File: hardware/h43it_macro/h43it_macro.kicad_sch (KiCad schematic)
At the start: 25 parts, among them J1 Conn_01x04_Pin, SW1 SW_Push, SW2 SW_Push

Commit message: updates
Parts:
- added D17, D18, D19, D20, D21, D22, D23, D24, D25, D26, D27, D28, D29, D30, D31, D32: LED, LED_SMD:LED_0805_2012Metric, symbol Device:LED
- added U1: ATtiny816-M, Package_DFN_QFN:VQFN-20-1EP_3x3mm_P0.4mm_EP1.7x1.7mm, symbol MCU_Microchip_ATtiny:ATtiny816-M
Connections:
- net A+: now also R1.2; no longer R1.1
- net B+: now also R2.2; no longer R2.1
- net C+: now also R3.2; no longer R3.1
- net D+: now also R4.2; no longer R4.1
- net GND: now also U1.21 (GND), U1.3 (GND)
- net M-: now also D21.1 (K), D29.1 (K); no longer D5.1 (K), D9.1 (K)
- net N-: now also D22.1 (K), D30.1 (K); no longer D10.1 (K), D6.1 (K)
- net O-: now also D23.1 (K), D31.1 (K); no longer D11.1 (K), D7.1 (K)
- net P-: now also D24.1 (K), D32.1 (K); no longer D12.1 (K), D8.1 (K)
- net TX: now also U1.12 (PB2)
- net UPDI: now also U1.19 (~{RESET}/PA0)
- net VCC: now also U1.4 (VCC)
- net at D10.2 (A), D11.2 (A), D12.2 (A)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: now also D13.2 (A), D14.2 (A), D15.2 (A), D16.2 (A), R2.1; no longer R3.2
- net at D1.2 (A), D2.2 (A), D3.2 (A)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: now also D5.2 (A), D6.2 (A), D7.2 (A), D8.2 (A), R1.1; no longer R1.2
- new net: D17.2 (A), D18.2 (A), D19.2 (A), D20.2 (A), D21.2 (A), D22.2 (A), D23.2 (A), D24.2 (A), R3.1
- new net: D25.2 (A), D26.2 (A), D27.2 (A), D28.2 (A), D29.2 (A), D30.2 (A), D31.2 (A), D32.2 (A), R4.1
- new net Q-: D17.1 (K), D25.1 (K), D5.1 (K), D9.1 (K)
- new net R-: D10.1 (K), D18.1 (K), D26.1 (K), D6.1 (K)
- new net S-: D11.1 (K), D19.1 (K), D27.1 (K), D7.1 (K)
- new net T-: D12.1 (K), D20.1 (K), D28.1 (K), D8.1 (K)
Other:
- moved on the sheet: D1, D2, D3, D4, R1

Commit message: schematic draft finsihed
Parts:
- added D33: LED, LED_SMD:LED_0805_2012Metric, symbol Device:LED
- added R5: 100Ω, Resistor_SMD:R_0805_2012Metric, symbol Device:R_US
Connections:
- net A+: now also U1.15 (PC0)
- net B+: now also U1.16 (PC1)
- net C+: now also U1.17 (PC2)
- net D+: now also U1.18 (PC3)
- net GND: now also D33.1 (K)
- net M-: now also U1.14 (PB0)
- net N-: now also U1.13 (PB1)
- net O-: now also U1.12 (PB2)
- net P-: now also U1.11 (PB3)
- net Q-: now also U1.10 (PB4)
- net R-: now also U1.9 (PB5)
- net S-: now also U1.7 (PA6)
- net SW: now also U1.5 (PA4)
- net T-: now also U1.8 (PA7)
- net TX: now also U1.20 (PA1); no longer U1.12 (PB2)
- net LED_ind: now reaches U1.6 (PA5)
- net LED_ind: now also R5.2
- new net: D33.2 (A), R5.1
- no-connect marks 0 -> 2
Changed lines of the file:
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@@
   (junction (at 81.28 157.48) (diameter 0) (color 0 0 0 0)
   )
-  (wire (pts (xy 184.15 109.22) (xy 181.61 109.22))
-    (stroke (width 0) (type default))
-  )
+  (no_connect (at 181.61 88.9))
+  (no_connect (at 181.61 86.36))
   (wire (pts (xy 48.26 107.95) (xy 52.07 107.95))
     (stroke (width 0) (type default))
@@
     (stroke (width 0) (type default))
   )
+  (wire (pts (xy 191.77 44.45) (xy 187.96 44.45))
+    (stroke (width 0) (type default))
+  )
   (wire (pts (xy 132.08 44.45) (xy 133.35 44.45))
     (stroke (width 0) (type default))
@@
     (effects (font (size 1.27 1.27)) (justify left bottom))
   )
-  (label "TX" (at 184.15 109.22 0) (fields_autoplaced)
+  (label "N-" (at 181.61 106.68 0) (fields_autoplaced)
+    (effects (font (size 1.27 1.27)) (justify left bottom))
+  )
+  (label "TX" (at 181.61 83.82 0) (fields_autoplaced)
     (effects (font (size 1.27 1.27)) (justify left bottom))
   )
@@
     (effects (font (size 1.27 1.27)) (justify left bottom))
   )
+  (label "GND" (at 191.77 44.45 0) (fields_autoplaced)
+    (effects (font (size 1.27 1.27)) (justify left bottom))
+  )
   (label "T-" (at 50.8 182.88 0) (fields_autoplaced)
     (effects (font (size 1.27 1.27)) (justify left bottom))
@@
     (effects (font (size 1.27 1.27)) (justify left bottom))
   )
+  (label "SW" (at 181.61 91.44 0) (fields_autoplaced)
+    (effects (font (size 1.27 1.27)) (justify left bottom))
+  )
   (label "B+" (at 39.37 82.55 0) (fields_autoplaced)
     (effects (font (size 1.27 1.27)) (justify left bottom))
   )
+  (label "O-" (at 181.61 109.22 0) (fields_autoplaced)
+    (effects (font (size 1.27 1.27)) (justify left bottom))
+  )
   (label "M-" (at 52.07 95.25 0) (fields_autoplaced)
     (effects (font (size 1.27 1.27)) (justify left bottom))
@@
     (effects (font (size 1.27 1.27)) (justify left bottom))
   )
+  (label "A+" (at 151.13 104.14 180) (fields_autoplaced)
+    (effects (font (size 1.27 1.27)) (justify right bottom))
+  )
   (label "T-" (at 69.85 182.88 0) (fields_autoplaced)
     (effects (font (size 1.27 1.27)) (justify left bottom))
@@
     (effects (font (size 1.27 1.27)) (justify left bottom))
   )
+  (label "S-" (at 181.61 96.52 0) (fields_autoplaced)
+    (effects (font (size 1.27 1.27)) (justify left bottom))
+  )
   (label "S-" (at 29.21 170.18 0) (fields_autoplaced)
     (effects (font (size 1.27 1.27)) (justify left bottom))
@@
     (effects (font (size 1.27 1.27)) (justify left bottom))
   )
+  (label "P-" (at 181.61 111.76 0) (fields_autoplaced)
+    (effects (font (size 1.27 1.27)) (justify left bottom))
+  )
+  (label "Q-" (at 181.61 114.3 0) (fields_autoplaced)
+    (effects (font (size 1.27 1.27)) (justify left bottom))
+  )
+  (label "D+" (at 151.13 111.76 180) (fields_autoplaced)
+    (effects (font (size 1.27 1.27)) (justify right bottom))
+  )
   (label "A+" (at 17.78 82.55 0) (fields_autoplaced)
     (effects (font (size 1.27 1.27)) (justify left bottom))
@@
     (effects (font (size 1.27 1.27)) (justify left bottom))
   )
+  (label "T-" (at 181.61 99.06 0) (fields_autoplaced)
+    (effects (font (size 1.27 1.27)) (justify left bottom))
+  )
+  (label "LED_ind" (at 181.61 93.98 0) (fields_autoplaced)
+    (effects (font (size 1.27 1.27)) (justify left bottom))
+  )
   (label "N-" (at 30.48 107.95 0) (fields_autoplaced)
     (effects (font (size 1.27 1.27)) (justify left bottom))
@@
     (effects (font (size 1.27 1.27)) (justify left bottom))
   )
+  (label "C+" (at 151.13 109.22 180) (fields_autoplaced)
+    (effects (font (size 1.27 1.27)) (justify right bottom))
+  )
   (label "O-" (at 71.12 120.65 0) (fields_autoplaced)
     (effects (font (size 1.27 1.27)) (justify left bottom))
   )
+  (label "B+" (at 151.13 106.68 180) (fields_autoplaced)
+    (effects (font (size 1.27 1.27)) (justify right bottom))
+  )
+  (label "LED_ind" (at 172.72 44.45 180) (fields_autoplaced)
+    (effects (font (size 1.27 1.27)) (justify right bottom))
+  )
+  (label "M-" (at 181.61 104.14 0) (fields_autoplaced)
+    (effects (font (size 1.27 1.27)) (justify left bottom))
+  )
   (label "UPDI" (at 181.61 81.28 0) (fields_autoplaced)
     (effects (font (size 1.27 1.27)) (justify left bottom))
@@
   )
   (label "M-" (at 30.48 95.25 0) (fields_autoplaced)
+    (effects (font (size 1.27 1.27)) (justify left bottom))
+  )
+  (label "R-" (at 181.61 116.84 0) (fields_autoplaced)
     (effects (font (size 1.27 1.27)) (justify left bottom))
   )
@@
     )
   )
+  (symbol (lib_id "Device:LED") (at 184.15 44.45 180) (unit 1)
+    (in_bom yes) (on_board yes) (dnp no) (fields_autoplaced)
+    (property "Reference" "D33" (at 185.7375 50.8 0)
+      (effects (font (size 1.27 1.27)))
+    )
+    (property "Value" "LED" (at 185.7375 48.26 0)
+      (effects (font (size 1.27 1.27)))
+    )
+    (property "Footprint" "LED_SMD:LED_0805_2012Metric" (at 184.15 44.45 0)
+      (effects (font (size 1.27 1.27)) hide)
+    )
+    (property "Datasheet" "~" (at 184.15 44.45 0)
+      (effects (font (size 1.27 1.27)) hide)
+    )
+    (pin "2")
+    (pin "1")
+    (instances
+      (project "h43it_macro"
+        (path "/37d2c260-87ad-48ae-8c36-e59ae5413c59"
+          (reference "D33") (unit 1)
+        )
+      )
+    )
+  )
   (symbol (lib_id "Device:LED") (at 86.36 120.65 180) (unit 1)
     (in_bom yes) (on_board yes) (dnp no) (fields_autoplaced)
@@
         )
       )
+    )
+  )
+  (symbol (lib_id "Device:R_US") (at 176.53 44.45 270) (unit 1)
+    (in_bom yes) (on_board yes) (dnp no) (fields_autoplaced)
+    (property "Reference" "R5" (at 176.53 38.1 90)
+      (effects (font (size 1.27 1.27)))
+    )
+    (property "Value" "100Ω" (at 176.53 40.64 90)
+      (effects (font (size 1.27 1.27)))
+    )
+    (property "Footprint" "Resistor_SMD:R_0805_2012Metric" (at 176.276 45.466 90)
+      (effects (font (size 1.27 1.27)) hide)
+    )
+    (property "Datasheet" "~" (at 176.53 44.45 0)
+      (effects (font (size 1.27 1.27)) hide)
+    )
+    (pin "1")
+    (pin "2")
+    (instances
+      (project "h43it_macro"
+        (path "/37d2c260-87ad-48ae-8c36-e59ae5413c59"
+          (reference "R5") (unit 1)
+        )
+      )

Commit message: schematic draft finsihed
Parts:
- removed SW1: SW_Push, MyLib:PTS526 SM15 SMTR2 LFS, symbol Switch:SW_Push
- BT1: footprint MyLib:BAT-HLD-001 -> MyLib:Battery_holder_AAA_534-2479
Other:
- moved on the sheet: SW2
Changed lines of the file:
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@@
   (junction (at 17.78 144.78) (diameter 0) (color 0 0 0 0)
   )
-  (junction (at 132.08 44.45) (diameter 0) (color 0 0 0 0)
-  )
   (junction (at 81.28 133.35) (diameter 0) (color 0 0 0 0)
   )
@@
   )
   (junction (at 166.37 124.46) (diameter 0) (color 0 0 0 0)
-  )
-  (junction (at 146.05 44.45) (diameter 0) (color 0 0 0 0)
   )
   (junction (at 39.37 95.25) (diameter 0) (color 0 0 0 0)
@@
     (stroke (width 0) (type default))
   )
-  (wire (pts (xy 146.05 54.61) (xy 146.05 44.45))
-    (stroke (width 0) (type default))
-  )
   (wire (pts (xy 40.64 40.64) (xy 55.88 40.64))
     (stroke (width 0) (type default))
@@
     (stroke (width 0) (type default))
   )
-  (wire (pts (xy 146.05 44.45) (xy 143.51 44.45))
-    (stroke (width 0) (type default))
-  )
   (wire (pts (xy 81.28 120.65) (xy 82.55 120.65))
     (stroke (width 0) (type default))
@@
     (stroke (width 0) (type default))
   )
-  (wire (pts (xy 149.86 44.45) (xy 146.05 44.45))
+  (wire (pts (xy 143.51 44.45) (xy 149.86 44.45))
     (stroke (width 0) (type default))
   )
@@
     (stroke (width 0) (type default))
   )
-  (wire (pts (xy 132.08 44.45) (xy 133.35 44.45))
+  (wire (pts (xy 129.54 44.45) (xy 133.35 44.45))
     (stroke (width 0) (type default))
   )
@@
     (stroke (width 0) (type default))
   )
-  (wire (pts (xy 143.51 54.61) (xy 146.05 54.61))
-    (stroke (width 0) (type default))
-  )
   (wire (pts (xy 88.9 170.18) (xy 92.71 170.18))
     (stroke (width 0) (type default))
@@
     (stroke (width 0) (type default))
   )
-  (wire (pts (xy 129.54 44.45) (xy 132.08 44.45))
-    (stroke (width 0) (type default))
-  )
   (wire (pts (xy 17.78 170.18) (xy 17.78 182.88))
     (stroke (width 0) (type default))
@@
     (stroke (width 0) (type default))
   )
-  (wire (pts (xy 132.08 54.61) (xy 132.08 44.45))
-    (stroke (width 0) (type default))
-  )
   (wire (pts (xy 81.28 170.18) (xy 81.28 182.88))
     (stroke (width 0) (type default))
@@
   )
   (wire (pts (xy 58.42 107.95) (xy 58.42 120.65))
-    (stroke (width 0) (type default))
-  )
-  (wire (pts (xy 133.35 54.61) (xy 132.08 54.61))
     (stroke (width 0) (type default))
   )
@@
         (path "/37d2c260-87ad-48ae-8c36-e59ae5413c59"
           (reference "D16") (unit 1)
-        )
-      )
-    )
-  )
-  (symbol (lib_id "Switch:SW_Push") (at 138.43 44.45 0) (unit 1)
-    (in_bom yes) (on_board yes) (dnp no) (fields_autoplaced)
-    (property "Reference" "SW1" (at 138.43 36.83 0)
-      (effects (font (size 1.27 1.27)))
-    )
-    (property "Value" "SW_Push" (at 138.43 39.37 0)
-      (effects (font (size 1.27 1.27)))
-    )
-    (property "Footprint" "MyLib:PTS526 SM15 SMTR2 LFS" (at 138.43 39.37 0)
-      (effects (font (size 1.27 1.27)) hide)
-    )
-    (property "Datasheet" "~" (at 138.43 39.37 0)
-      (effects (font (size 1.27 1.27)) hide)
-    )
-    (pin "2")
-    (pin "1")
-    (instances
-      (project "h43it_macro"
-        (path "/37d2c260-87ad-48ae-8c36-e59ae5413c59"
-          (reference "SW1") (unit 1)
         )
       )
@@
       (effects (font (size 1.27 1.27)) (justify left))
     )
-    (property "Footprint" "MyLib:BAT-HLD-001" (at 55.88 44.196 90)
+    (property "Footprint" "MyLib:Battery_holder_AAA_534-2479" (at 55.88 44.196 90)
       (effects (font (size 1.27 1.27)) hide)
     )
@@
     )
   )
-  (symbol (lib_id "Switch:SW_Push") (at 138.43 54.61 0) (unit 1)
-    (in_bom yes) (on_board yes) (dnp no) (fields_autoplaced)
-    (property "Reference" "SW2" (at 138.43 46.99 0)
-      (effects (font (size 1.27 1.27)))
-    )
-    (property "Value" "SW_Push" (at 138.43 49.53 0)
-      (effects (font (size 1.27 1.27)))
-    )
-    (property "Footprint" "MyLib:FSM2JSMAATR" (at 138.43 49.53 0)
-      (effects (font (size 1.27 1.27)) hide)
-    )
-    (property "Datasheet" "~" (at 138.43 49.53 0)
-      (effects (font (size 1.27 1.27)) hide)
-    )
+  (symbol (lib_id "Switch:SW_Push") (at 138.43 44.45 0) (unit 1)
+    (in_bom yes) (on_board yes) (dnp no) (fields_autoplaced)
+    (property "Reference" "SW2" (at 138.43 36.83 0)
+      (effects (font (size 1.27 1.27)))
+    )
+    (property "Value" "SW_Push" (at 138.43 39.37 0)
+      (effects (font (size 1.27 1.27)))
+    )
+    (property "Footprint" "MyLib:FSM2JSMAATR" (at 138.43 39.37 0)
+      (effects (font (size 1.27 1.27)) hide)
+    )
+    (property "Datasheet" "~" (at 138.43 39.37 0)
+      (effects (font (size 1.27 1.27)) hide)
+    )

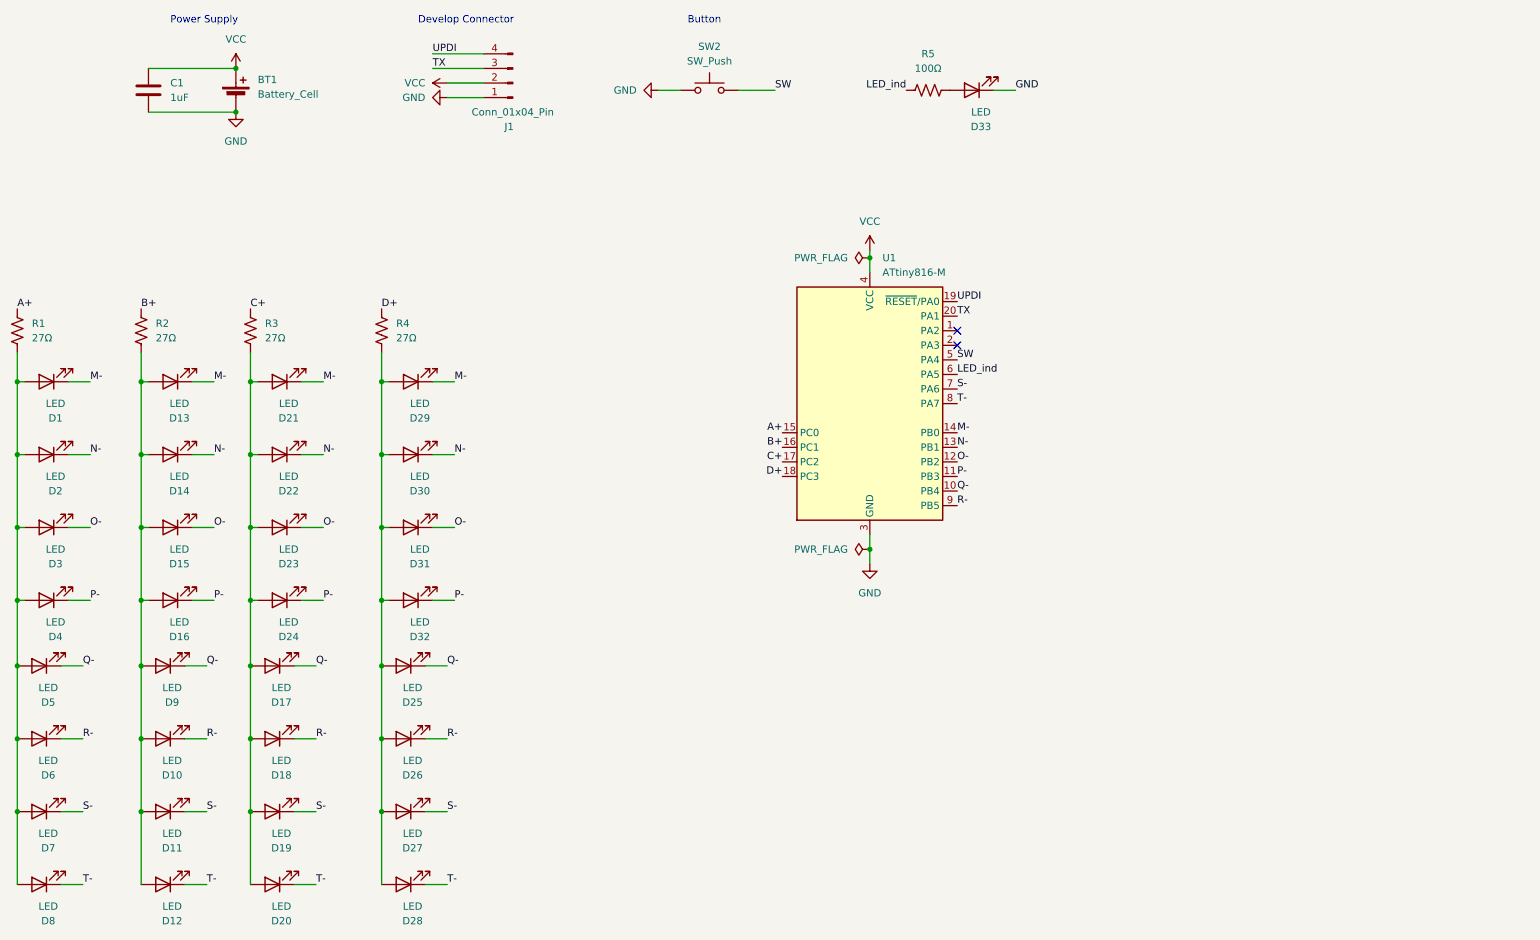
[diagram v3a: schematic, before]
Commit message: add twin attiny 816
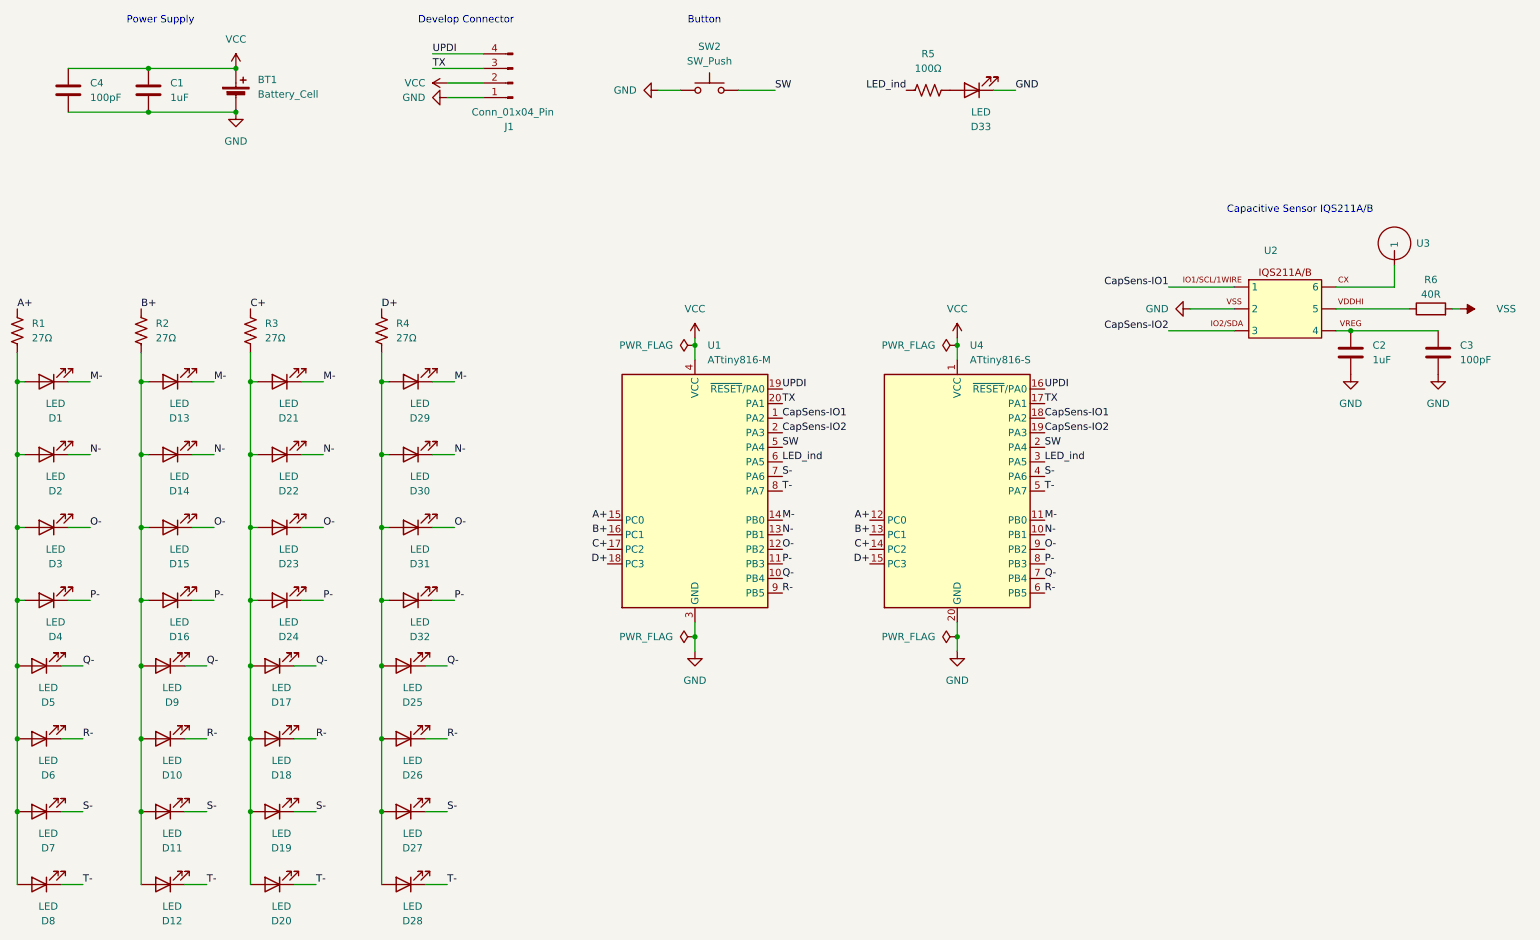
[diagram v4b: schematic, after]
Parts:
- added C2: 1uF, symbol Device:C
- added C3: 100pF, symbol Device:C
- added C4: 100pF, Capacitor_SMD:C_0805_2012Metric, symbol Device:C
- added R6: 40R, symbol Device:R
- added U2: ~, symbol MySymLib:Azoteq-IQS211A/B
- added U3: ~, symbol MySymLib:Self-Capacitive-Pad_V1
- added U4: ATtiny816-S, Package_SO:SOIC-20W_7.5x12.8mm_P1.27mm, symbol MCU_Microchip_ATtiny:ATtiny816-S
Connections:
- net A+: now also U4.12 (PC0)
- net B+: now also U4.13 (PC1)
- net C+: now also U4.14 (PC2)
- net D+: now also U4.15 (PC3)
- net GND: now also C2.2, C3.2, C4.2, U2. (6), U4.20 (GND)
- net LED_ind: now also U4.3 (PA5)
- net M-: now also U4.11 (PB0)
- net N-: now also U4.10 (PB1)
- net O-: now also U4.9 (PB2)
- net P-: now also U4.8 (PB3)
- net Q-: now also U4.7 (PB4)
- net R-: now also U4.6 (PB5)
- net S-: now also U4.4 (PA6)
- net SW: now also U4.2 (PA4)
- net T-: now also U4.5 (PA7)
- net TX: now also U4.17 (PA1)
- net UPDI: now also U4.16 (~{RESET}/PA0)
- net VCC: now also C4.1, U4.1 (VCC)
- net CapSens-IO1: now reaches U1.1 (PA2)
- net CapSens-IO1: now also U2. (6), U4.18 (PA2)
- net CapSens-IO2: now reaches U1.2 (PA3)
- net CapSens-IO2: now also U2. (6), U4.19 (PA3)
- new net: C2.1, C3.1, U2. (6)
- new net: U2. (6), U3. (1)
- new net: R6.1, U2. (6)
- new net VSS: R6.2
- no-connect marks 2 -> 0
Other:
- note added: "Capacitive Sensor IQS211A/B"
- moved on the sheet: U1

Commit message: pcb for macro
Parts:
- removed U1: ATtiny816-M, Package_DFN_QFN:VQFN-20-1EP_3x3mm_P0.4mm_EP1.7x1.7mm, symbol MCU_Microchip_ATtiny:ATtiny816-M
- removed U3: ~, symbol MySymLib:Self-Capacitive-Pad_V1
- added U6: ~, MyLib:TouchButton-15x10mm, symbol MySymLib:Self-Capacitive-Pad_V1
- BT1: footprint MyLib:Battery_holder_AAA_534-2479 -> MyLib:Battery_holder__Keystone_Electronic_AA_2462
- C2: value 1uF -> 100pF; footprint (none) -> Capacitor_SMD:C_0805_2012Metric
- C3: value 100pF -> 1uF; footprint (none) -> Capacitor_SMD:C_0805_2012Metric
- R5: value 100Ω -> 27Ω
- U2: footprint (none) -> MyLib:TSOT32-6
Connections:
- net CapSens-IO1: now also U2.1 (IO1); no longer U2. (6)
- net CapSens-IO2: now also U2.3 (IO2); no longer U2. (6)
- net GND: now also U2.2 (VSS); no longer U2. (6)
- net at C2.1, C3.1: now also U2.4 (VREG); no longer U2. (6)
- net at R6.1: now also U2.5 (VDDHI); no longer U2. (6)
- new net: U2.6 (CX), U6.1
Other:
- moved on the sheet: R6, U2, U4

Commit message: pcb for macro
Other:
- moved on the sheet: C2, C3, R6, U2, U4, U6

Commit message: pcb for macro 3
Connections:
- net CapSens-IO1: now also U4.2 (PA4); no longer U4.18 (PA2)
- net SW: now also U4.18 (PA2); no longer U4.2 (PA4)
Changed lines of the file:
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@@
     (effects (font (size 1.27 1.27)) (justify left bottom))
   )
-  (label "CapSens-IO1" (at 138.43 106.68 0) (fields_autoplaced)
+  (label "CapSens-IO1" (at 138.43 111.76 0) (fields_autoplaced)
     (effects (font (size 1.27 1.27)) (justify left bottom))
   )
@@
     (effects (font (size 1.27 1.27)) (justify left bottom))
   )
-  (label "SW" (at 138.43 111.76 0) (fields_autoplaced)
+  (label "SW" (at 138.43 106.68 0) (fields_autoplaced)
     (effects (font (size 1.27 1.27)) (justify left bottom))
   )

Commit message: tiny changes and added R6
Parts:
- added CapSens-IO1: SolderJumper_2_Bridged, Jumper:SolderJumper-2_P1.3mm_Bridged_RoundedPad1.0x1.5mm, symbol Jumper:SolderJumper_2_Bridged
- added CapSens_IO2, SWITCH1: SolderJumper_2_Open, Jumper:SolderJumper-2_P1.3mm_Open_RoundedPad1.0x1.5mm, symbol Jumper:SolderJumper_2_Open
- R6: value 40R -> 42R; footprint (none) -> Resistor_SMD:R_0805_2012Metric
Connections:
- net CapSens-IO1: now also CapSens-IO1.2 (B)
- net CapSens-IO2: now also CapSens_IO2.2 (B); no longer U4.19 (PA3)
- net SW: now also U4.19 (PA3), SWITCH1.2 (B); no longer U4.18 (PA2)
- new net interrupt_pin: CapSens-IO1.1 (A), CapSens_IO2.1 (A), SWITCH1.1 (A), U4.18 (PA2)
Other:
- moved on the sheet: C2, C3, R6, U2, U6
